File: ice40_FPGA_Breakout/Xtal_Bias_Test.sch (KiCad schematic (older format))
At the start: 61 parts, among them J4 4POS_JUMPER, J5 4POS_JUMPER, J6 4POS_JUMPER, J7 4POS_JUMPER, J8 4POS_JUMPER, U7 MIC53x4, X1 OSC_4-SMD, X2 OSC_6-SMD

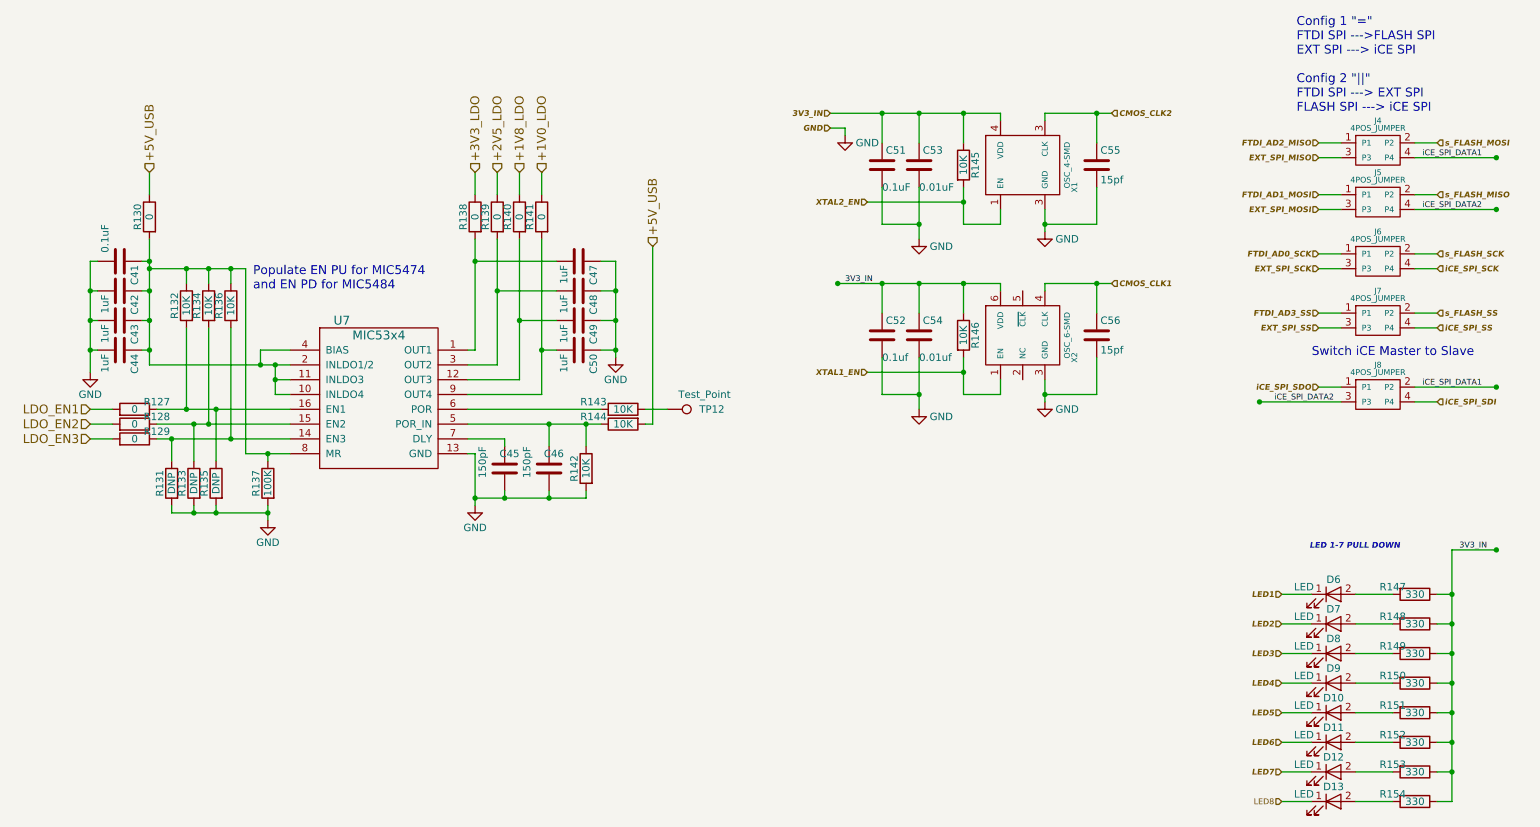
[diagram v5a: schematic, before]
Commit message: schematic clean up, label aligned
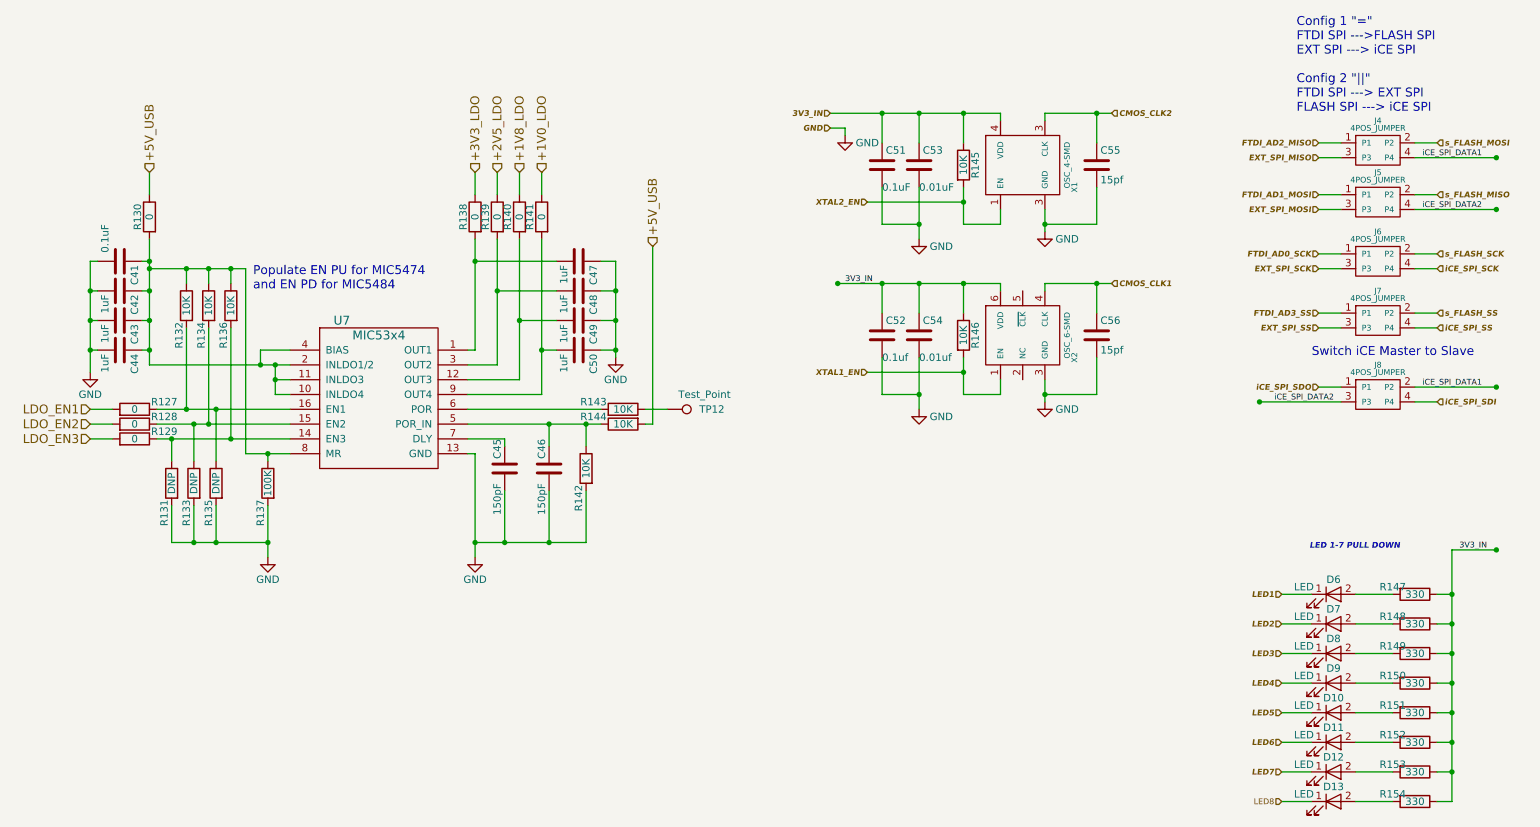
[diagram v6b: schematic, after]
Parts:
- C41, C45, C46, C51, C52, C53, C54, C55, C56: footprint (none) -> Capacitor_SMD:C_0402_1005Metric
- C42, C43, C44, C47, C48, C49, C50: footprint (none) -> Capacitor_SMD:C_0603_1608Metric
- D10, D11, D12, D13, D6, D7, D8, D9: footprint (none) -> LED_SMD:LED_0402_1005Metric
- J4, J5, J6, J7, J8: footprint (none) -> Conn_PinHeader_2.00mm:PinHeader_2x02_P2.00mm_Vertical
- R127, R128, R129, R131, R132, R133, R134, R135, R136, R137, R142, R143, R144, R145, R146, R147, R148, R149, R150, R151, R152, R153, R154: footprint (none) -> Resistor_SMD:R_0402_1005Metric
- R130, R138, R139, R140, R141: footprint (none) -> Resistor_SMD:R_0603_1608Metric
- TP12: footprint (none) -> Conn_PinHeader_2.00mm:PinHeader_1x01_P2.00mm_Vertical

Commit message: assigned footprint to each component
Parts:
- J4, J5, J6, J7, J8: footprint Conn_PinHeader_2.00mm:PinHeader_2x02_P2.00mm_Vertical -> Connector_PinHeader_2.00mm:PinHeader_2x02_P2.00mm_Vertical
- TP12: footprint Conn_PinHeader_2.00mm:PinHeader_1x01_P2.00mm_Vertical -> TestPoint:TestPoint_Pad_D2.0mm
- U7: footprint (none) -> Package_DFN_QFN:QFN-16-1EP_4x4mm_P0.65mm_EP2.5x2.5mm
- X1: footprint (none) -> Crystal:Crystal_SMD_Abracon_ABM8G-4Pin_3.2x2.5mm
- X2: footprint (none) -> GTI_Footprint_Lib:OSC_6-SMD_NO-LEAD
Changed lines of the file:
@@
 F 0 "X2" V 7950 2550 39  0000 C CNN
 F 1 "OSC_6-SMD" V 7900 2700 39  0000 C CNN
-F 2 "" H 7600 2700 39  0001 C CNN
+F 2 "GTI_Footprint_Lib:OSC_6-SMD_NO-LEAD" H 7600 2700 39  0001 C CNN
 F 3 "" H 7600 2700 39  0001 C CNN
 	1    7600 2700
@@
 	7200 2350 7200 2550
 Wire Wire Line
-	6350 2350 6650 2350
-Wire Wire Line
-	6650 2350 6900 2350
-Wire Wire Line
-	6900 2350 7200 2350
-Wire Wire Line
-	7200 2350 7450 2350
+	6350 2350 7450 2350
 Wire Wire Line
 	7450 2350 7450 2400
 Wire Wire Line
-	7200 2850 7200 2950
-Wire Wire Line
-	7200 2950 7200 3100
+	7200 2850 7200 3100
 Wire Wire Line
 	7200 3100 7450 3100
@@
 	7450 3100 7450 3000
 Wire Wire Line
-	7750 3000 7750 3100
-Wire Wire Line
-	7750 3100 7750 3150
+	7750 3000 7750 3150
 Wire Wire Line
 	7750 2400 7750 2350
 Wire Wire Line
-	7750 2350 8100 2350
-Wire Wire Line
-	8100 2350 8200 2350
+	7750 2350 8200 2350
 Wire Wire Line
 	8100 2350 8100 2550
@@
 Connection ~ 7200 2350
 Wire Wire Line
-	6900 2850 6900 3100
-Wire Wire Line
-	6900 3100 6900 3200
+	6900 2850 6900 3200
 Wire Wire Line
 	6650 2550 6650 2350
@@
 	7200 1200 7200 1400
 Wire Wire Line
-	6300 1200 6650 1200
-Wire Wire Line
-	6650 1200 6900 1200
-Wire Wire Line
-	6900 1200 7200 1200
-Wire Wire Line
-	7200 1200 7450 1200
+	6300 1200 7450 1200
 Wire Wire Line
 	7450 1200 7450 1250
 Wire Wire Line
-	7200 1700 7200 1800
-Wire Wire Line
-	7200 1800 7200 1950
+	7200 1700 7200 1950
 Wire Wire Line
 	7200 1950 7450 1950
@@
 	7450 1950 7450 1850
 Wire Wire Line
-	7750 1850 7750 1950
-Wire Wire Line
-	7750 1950 7750 2000
+	7750 1850 7750 2000
 Wire Wire Line
 	7750 1250 7750 1200
 Wire Wire Line
-	7750 1200 8100 1200
-Wire Wire Line
-	8100 1200 8200 1200
+	7750 1200 8200 1200
 Wire Wire Line
 	8100 1200 8100 1400
@@
 Connection ~ 7200 1200
 Wire Wire Line
-	6900 1700 6900 1950
-Wire Wire Line
-	6900 1950 6900 2050
+	6900 1700 6900 2050
 Wire Wire Line
 	6650 1400 6650 1200
@@
 F 0 "X1" V 7950 1400 39  0000 C CNN
 F 1 "OSC_4-SMD" V 7900 1550 39  0000 C CNN
-F 2 "" H 7600 1550 39  0001 C CNN
+F 2 "Crystal:Crystal_SMD_Abracon_ABM8G-4Pin_3.2x2.5mm" H 7600 1550 39  0001 C CNN
 F 3 "" H 7600 1550 39  0001 C CNN
 	1    7600 1550
@@
 	10400 4450 10500 4450
 Wire Wire Line
-	10500 4150 10500 4450
-Wire Wire Line
-	10500 4450 10500 4650
-Wire Wire Line
-	10500 4650 10500 4850
-Wire Wire Line
-	10500 4850 10500 5050
-Wire Wire Line
-	10500 5050 10500 5250
-Wire Wire Line
-	10500 5250 10500 5450
-Wire Wire Line
-	10500 5450 10500 5650
-Wire Wire Line
-	10500 5650 10500 5850
+	10500 4150 10500 5850
 Wire Wire Line
 	10500 4650 10400 4650
@@
 F 0 "J4" H 10000 1250 39  0000 C CNN
 F 1 "4POS_JUMPER" H 10000 1200 39  0000 C CNN
-F 2 "Conn_PinHeader_2.00mm:PinHeader_2x02_P2.00mm_Vertical" H 10000 1250 39  0001 C CNN
+F 2 "Connector_PinHeader_2.00mm:PinHeader_2x02_P2.00mm_Vertical" H 10000 1250 39  0001 C CNN
 F 3 "" H 10000 1250 39  0001 C CNN
 	1    10000 1250
@@
 F 0 "J5" H 10000 1600 39  0000 C CNN
 F 1 "4POS_JUMPER" H 10000 1550 39  0000 C CNN
-F 2 "Conn_PinHeader_2.00mm:PinHeader_2x02_P2.00mm_Vertical" H 10000 1600 39  0001 C CNN
+F 2 "Connector_PinHeader_2.00mm:PinHeader_2x02_P2.00mm_Vertical" H 10000 1600 39  0001 C CNN
 F 3 "" H 10000 1600 39  0001 C CNN
 	1    10000 1600
@@
 F 0 "J6" H 10000 2000 39  0000 C CNN
 F 1 "4POS_JUMPER" H 10000 1950 39  0000 C CNN
-F 2 "Conn_PinHeader_2.00mm:PinHeader_2x02_P2.00mm_Vertical" H 10000 2000 39  0001 C CNN
+F 2 "Connector_PinHeader_2.00mm:PinHeader_2x02_P2.00mm_Vertical" H 10000 2000 39  0001 C CNN
 F 3 "" H 10000 2000 39  0001 C CNN
 	1    10000 2000
@@
 F 0 "J7" H 10000 2400 39  0000 C CNN
 F 1 "4POS_JUMPER" H 10000 2350 39  0000 C CNN
-F 2 "Conn_PinHeader_2.00mm:PinHeader_2x02_P2.00mm_Vertical" H 10000 2400 39  0001 C CNN
+F 2 "Connector_PinHeader_2.00mm:PinHeader_2x02_P2.00mm_Vertical" H 10000 2400 39  0001 C CNN
 F 3 "" H 10000 2400 39  0001 C CNN
 	1    10000 2400
@@
 F 0 "J8" H 10000 2900 39  0000 C CNN
 F 1 "4POS_JUMPER" H 10000 2850 39  0000 C CNN
-F 2 "Conn_PinHeader_2.00mm:PinHeader_2x02_P2.00mm_Vertical" H 10000 2900 39  0001 C CNN
+F 2 "Connector_PinHeader_2.00mm:PinHeader_2x02_P2.00mm_Vertical" H 10000 2900 39  0001 C CNN
 F 3 "" H 10000 2900 39  0001 C CNN
 	1    10000 2900
@@
 F 0 "U7" H 3000 2700 60  0000 C CNN
 F 1 "MIC53x4" H 3250 2600 60  0000 C CNN
-F 2 "" H 3250 2650 60  0001 C CNN
+F 2 "Package_DFN_QFN:QFN-16-1EP_4x4mm_P0.65mm_EP2.5x2.5mm" H 3250 2650 60  0001 C CNN
 F 3 "" H 3250 2650 60  0001 C CNN
 	1    3250 2650
@@
 F 0 "TP12" V 5200 3500 50  0000 C CNN
 F 1 "Test_Point" V 5100 3450 50  0000 C CNN
-F 2 "Conn_PinHeader_2.00mm:PinHeader_1x01_P2.00mm_Vertical" H 5400 3200 50  0001 C CNN
+F 2 "TestPoint:TestPoint_Pad_D2.0mm" H 5400 3200 50  0001 C CNN
 F 3 "" H 5400 3200 50  0001 C CNN
 	1    5200 3200
@@
 $EndComp
 Wire Wire Line
-	1700 2050 1700 2200
-Wire Wire Line
-	1700 2200 1700 2250
-Wire Wire Line
-	1700 2250 1700 2400
-Wire Wire Line
-	1700 2400 1700 2600
-Wire Wire Line
-	1700 2600 1700 2800
-Wire Wire Line
-	1700 2800 1700 2900
+	1700 2050 1700 2900
 Wire Wire Line
 	1700 2600 1650 2600
 Connection ~ 1700 2600
 Wire Wire Line
-	1700 2900 2450 2900
-Wire Wire Line
-	2450 2900 2550 2900
-Wire Wire Line
-	2550 2900 2650 2900
-Wire Wire Line
-	1300 2200 1300 2400
-Wire Wire Line
-	1300 2400 1300 2600
-Wire Wire Line
-	1300 2600 1300 2800
-Wire Wire Line
-	1300 2800 1300 2950
+	1700 2900 2650 2900
+Wire Wire Line
+	1300 2200 1300 2950
 Wire Wire Line
 	1350 2800 1300 2800
@@
 Connection ~ 1300 2600
 Wire Wire Line
-	2550 2900 2550 3000
-Wire Wire Line
-	2550 3000 2550 3100
+	2550 2900 2550 3100
 Connection ~ 2550 2900
 Connection ~ 2550 3000
@@
 	3900 2800 3850 2800
 Wire Wire Line
-	3900 2050 3900 2200
-Wire Wire Line
-	3900 2200 3900 2800
+	3900 2050 3900 2800
 Wire Wire Line
 	4050 2900 3850 2900
 Wire Wire Line
-	4050 2050 4050 2400
-Wire Wire Line
-	4050 2400 4050 2900
+	4050 2050 4050 2900
 Wire Wire Line
 	4200 3000 3850 3000
 Wire Wire Line
-	4200 2050 4200 2600
-Wire Wire Line
-	4200 2600 4200 3000
+	4200 2050 4200 3000
 Wire Wire Line
 	4350 3100 3850 3100
 Wire Wire Line
-	4350 2050 4350 2800
-Wire Wire Line
-	4350 2800 4350 3100
+	4350 2050 4350 3100
 Wire Wire Line
 	1650 2400 1700 2400
@@
 	4750 2200 4850 2200
 Wire Wire Line
-	4850 2200 4850 2400
-Wire Wire Line
-	4850 2400 4850 2600
-Wire Wire Line
-	4850 2600 4850 2800
-Wire Wire Line
-	4850 2800 4850 2850
+	4850 2200 4850 2850
 Wire Wire Line
 	4750 2800 4850 2800
@@
 	3850 3200 4750 3200
 Wire Wire Line
-	3850 3300 4400 3300
-Wire Wire Line
-	4400 3300 4650 3300
-Wire Wire Line
-	4650 3300 4750 3300
+	3850 3300 4750 3300
 Wire Wire Line
 	4100 3400 4100 3450
@@
 	3850 3500 3900 3500
 Wire Wire Line
-	3900 3500 3900 4100
-Wire Wire Line
-	3900 4100 3900 4200
+	3900 3500 3900 4200
 Connection ~ 3900 4100
 Wire Wire Line
@@
 	4650 4100 4650 3750
 Wire Wire Line
-	3900 4100 4100 4100
-Wire Wire Line
-	4100 4100 4400 4100
-Wire Wire Line
-	4400 4100 4650 4100
+	3900 4100 4650 4100
 Wire Wire Line
 	5050 3200 5200 3200
@@
 Connection ~ 2500 3500
 Wire Wire Line
-	2500 3850 2500 4100
-Wire Wire Line
-	2500 4100 2500 4200
+	2500 3850 2500 4200
 Wire Wire Line
 	1650 2200 1700 2200
@@
 	3850 3400 4100 3400
 Wire Wire Line
-	1750 3200 1950 3200
-Wire Wire Line
-	1950 3200 2150 3200
-Wire Wire Line
-	2150 3200 2650 3200
-Wire Wire Line
-	1750 3300 2000 3300
-Wire Wire Line
-	2000 3300 2100 3300
-Wire Wire Line
-	2100 3300 2650 3300
-Wire Wire Line
-	1750 3400 1850 3400
-Wire Wire Line
-	1850 3400 2250 3400
-Wire Wire Line
-	2250 3400 2650 3400
-Wire Wire Line
-	2350 3500 2500 3500
-Wire Wire Line
-	2500 3500 2650 3500
+	1750 3200 2650 3200
+Wire Wire Line
+	1750 3300 2650 3300
+Wire Wire Line
+	1750 3400 2650 3400
+Wire Wire Line
+	2350 3500 2650 3500
 Wire Wire Line
 	1950 2650 1950 3200
@@
 	1950 2350 1950 2250
 Wire Wire Line
-	1700 2250 1950 2250
-Wire Wire Line
-	1950 2250 2100 2250
-Wire Wire Line
-	2100 2250 2250 2250
-Wire Wire Line
-	2250 2250 2350 2250
+	1700 2250 2350 2250
 Wire Wire Line
 	2250 2250 2250 2350
@@
 	1850 3850 1850 4100
 Wire Wire Line
-	1850 4100 2000 4100
-Wire Wire Line
-	2000 4100 2150 4100
-Wire Wire Line
-	2150 4100 2500 4100
+	1850 4100 2500 4100
 Wire Wire Line
 	2150 4100 2150 3850
